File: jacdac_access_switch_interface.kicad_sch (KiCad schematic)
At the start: 43 parts

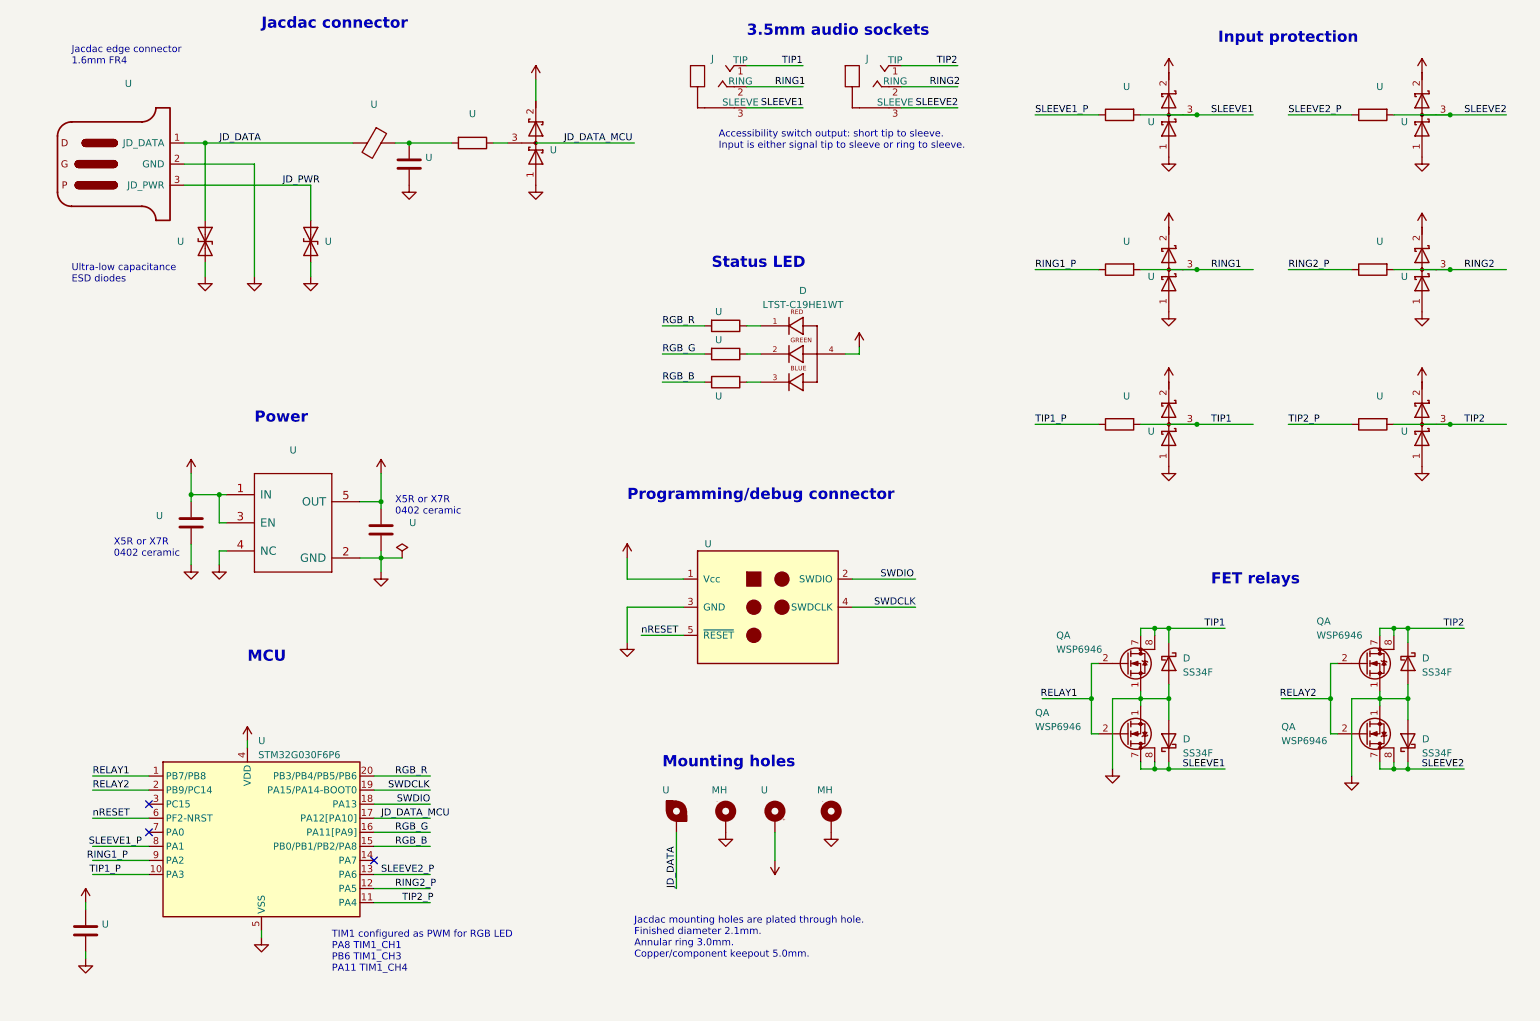
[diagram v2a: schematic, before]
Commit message: Added push button switch to enable flashing & orange status LED
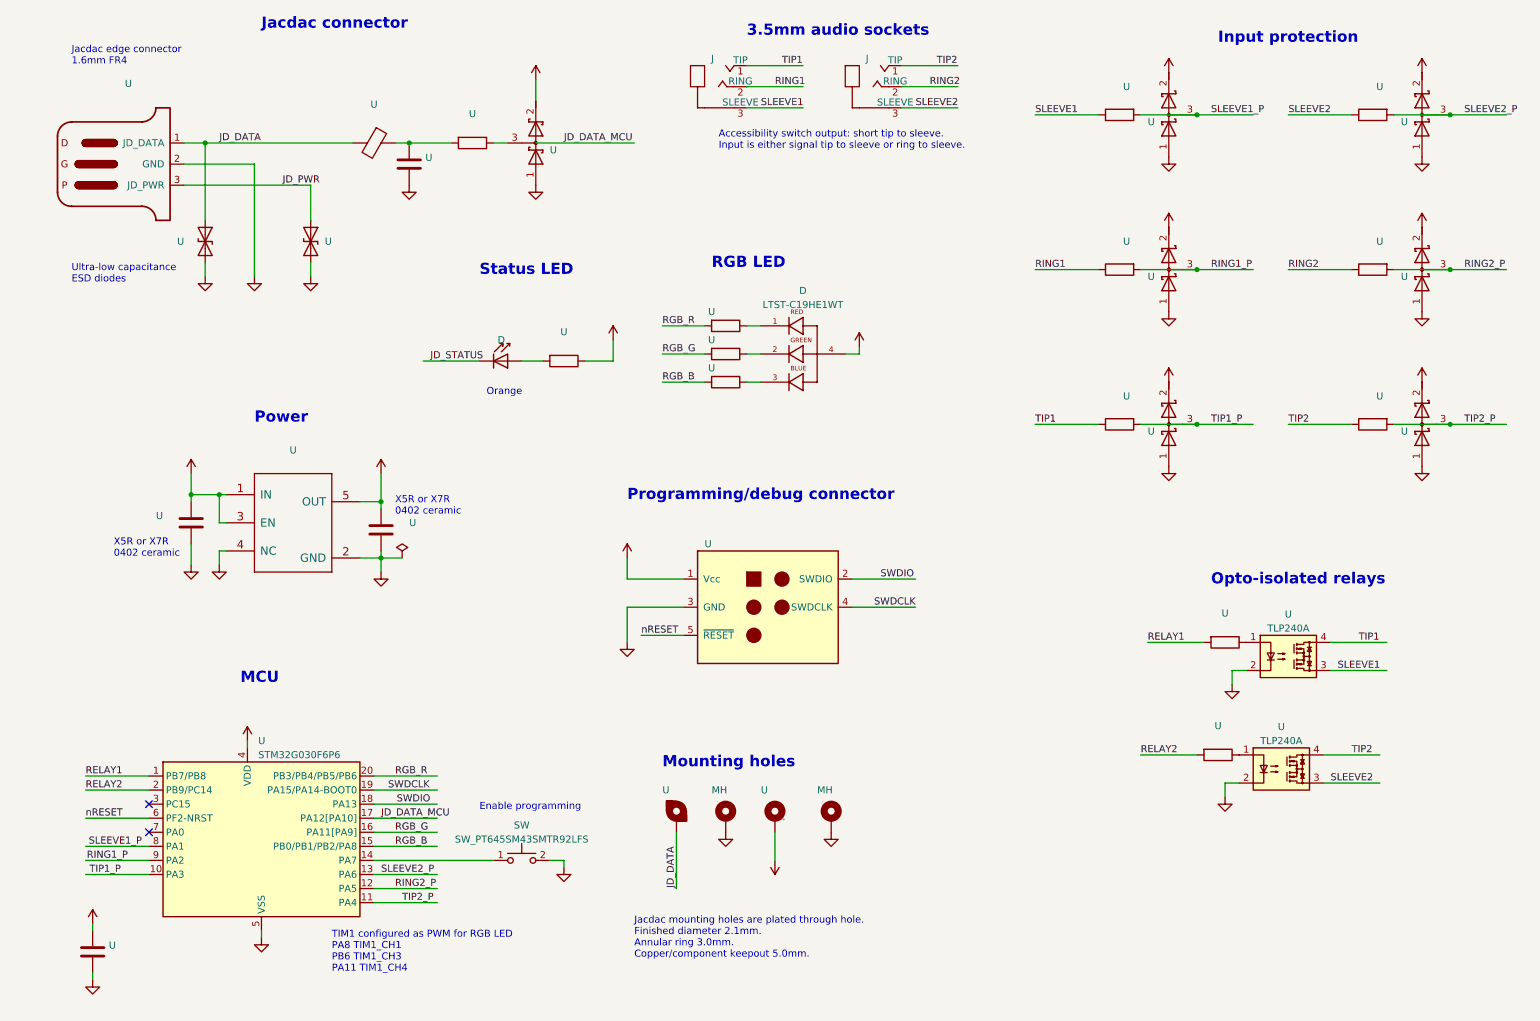
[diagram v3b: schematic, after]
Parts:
- removed D (x4): SS34F, jacdac_access_switch_interface:SMAF, symbol jacdac_access_switch_interface:SS34F
- removed Q (x4): WSP6946, jacdac_access_switch_interface:SOP-8_3.9x4.9mm_P1.27mm, symbol jacdac_access_switch_interface:WSP6946
- added D: LED_status, jacdac_access_switch_interface:LED_0603_1608Metric, symbol jacdac_access_switch_interface:LED_status
- added SW: SW_PT645SM43SMTR92LFS, jacdac_access_switch_interface:SW_SPST_PTS645, symbol jacdac_access_switch_interface:SW_PT645SM43SMTR92LFS
- added U (x3): (no value), symbol Device:R
- added U (x2): TLP240A, jacdac_access_switch_interface:LF1_TP1_TOSHIBA_11-5B201S, symbol jacdac_access_switch_interface:TLP240A
- U: LCSC C270649 -> C25105
- U: LCSC C270649 -> C25756
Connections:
- net +3V3: now also U.1
- net GND: now also SW.2, U.2, U.2
- net RELAY1: now also U.2
- net RELAY2: now also U.2
- net RING1: now also U.1; no longer U.2, U.3 (common)
- net RING1_P: now also U.2, U.3 (common); no longer U.1
- net RING2: now also U.1; no longer U.2, U.3 (common)
- net RING2_P: now also U.2, U.3 (common); no longer U.1
- net SLEEVE1: now also U.1, U.3; no longer U.2, U.3 (common)
- net SLEEVE1_P: now also U.2, U.3 (common); no longer U.1
- net SLEEVE2: now also U.1, U.3; no longer U.2, U.3 (common)
- net SLEEVE2_P: now also U.2, U.3 (common); no longer U.1
- net TIP1: now also U.1, U.4; no longer U.2, U.3 (common)
- net TIP1_P: now also U.2, U.3 (common); no longer U.1
- net TIP2: now also U.1, U.4; no longer U.2, U.3 (common)
- net TIP2_P: now also U.2, U.3 (common); no longer U.1
- net at U.14 (PA7): now also SW.1
- new net: D.2 (A), U.2
- new net: U.1, U.1 (x2)
- new net JD_STATUS: D.1 (K)
- no-connect marks 3 -> 2
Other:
- note added: "Enable programming"
- note added: "Opto-isolated relays"
- note added: "Orange"
- note added: "RGB LED"
- note removed: "FET relays"
- moved on the sheet: U

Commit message: Initial component placement for PCB
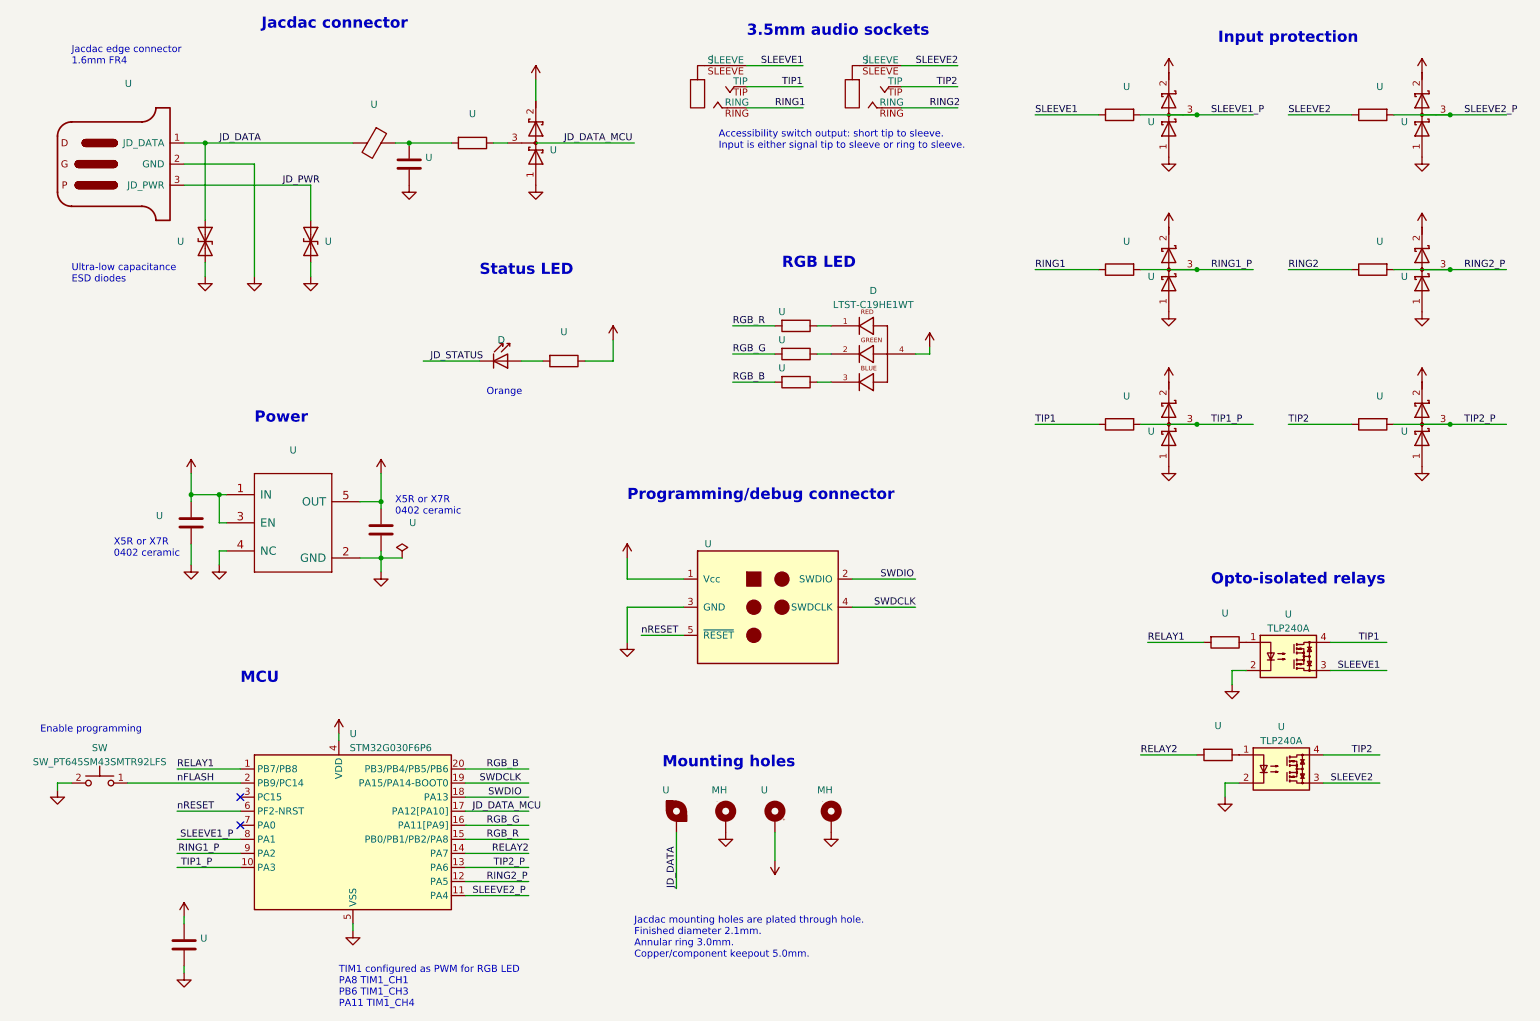
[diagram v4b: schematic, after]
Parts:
- removed J (x2): 54-00036_audio_plug, jacdac_access_switch_interface:Tensility-54-00036-0, symbol jacdac_access_switch_interface:54-00036_audio_plug
- added J (x2): jack_3.5_pj313d, jacdac_access_switch_interface:jack_3.5_pj313d_smt, symbol jacdac_access_switch_interface:jack_3.5_pj313d
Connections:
- net RELAY2: now also U.14 (PA7); no longer U.2 (PB9/PC14)
- net RGB_B: now also U.20 (PB3/PB4/PB5/PB6); no longer U.15 (PB0/PB1/PB2/PA8)
- net RGB_R: now also U.15 (PB0/PB1/PB2/PA8); no longer U.20 (PB3/PB4/PB5/PB6)
- net RING1: now also J.RING
- net RING2: now also J.RING
- net SLEEVE1: now also J.SLEEVE
- net SLEEVE2: now also J.SLEEVE
- net SLEEVE2_P: now also U.11 (PA4); no longer U.13 (PA6)
- net TIP1: now also J.TIP
- net TIP2: now also J.TIP
- net TIP2_P: now also U.13 (PA6); no longer U.11 (PA4)
- net nFLASH: now reaches SW.1
- net nFLASH: now also U.2 (PB9/PC14); no longer U.14 (PA7)
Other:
- moved on the sheet: D, SW, U

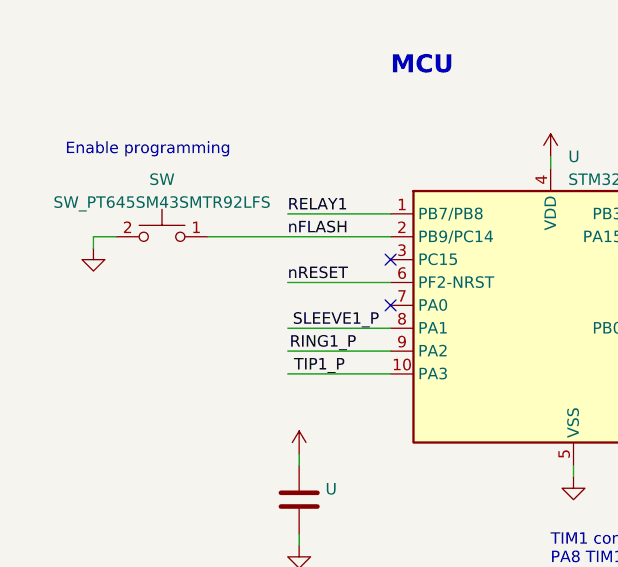
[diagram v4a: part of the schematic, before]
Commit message: Updated footprint identifiers, routing started
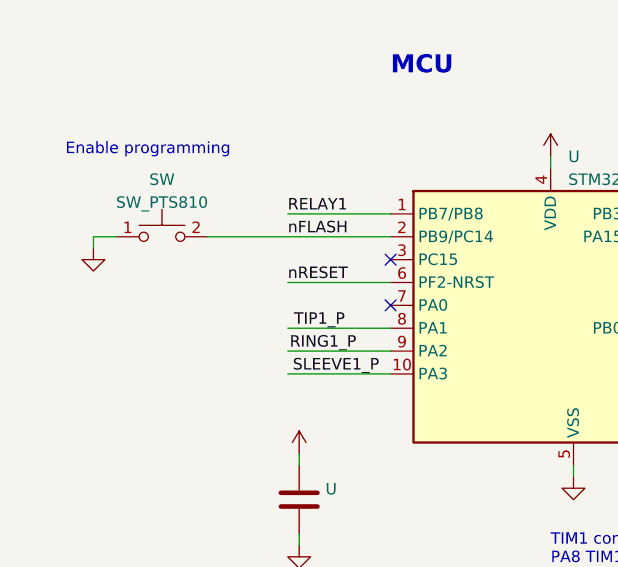
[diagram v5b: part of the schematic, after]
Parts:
- removed SW: SW_PT645SM43SMTR92LFS, jacdac_access_switch_interface:SW_SPST_PTS645, symbol jacdac_access_switch_interface:SW_PT645SM43SMTR92LFS
- added SW: SW_PTS810, jacdac_access_switch_interface:SW_SPST_PTS810, symbol jacdac_access_switch_interface:SW_PTS810
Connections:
- net GND: now also SW.1
- net SLEEVE1_P: now also U.10 (PA3); no longer U.8 (PA1)
- net TIP1_P: now also U.8 (PA1); no longer U.10 (PA3)
- net nFLASH: now also SW.2

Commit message: Routing in progress
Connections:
- net RELAY2: now also U.11 (PA4); no longer U.14 (PA7)
- net RING2_P: now also U.13 (PA6); no longer U.12 (PA5)
- net SLEEVE1: now also U.4; no longer U.3
- net SLEEVE2_P: now also U.12 (PA5); no longer U.11 (PA4)
- net TIP1: now also U.3; no longer U.4
- net TIP2_P: now also U.14 (PA7); no longer U.13 (PA6)

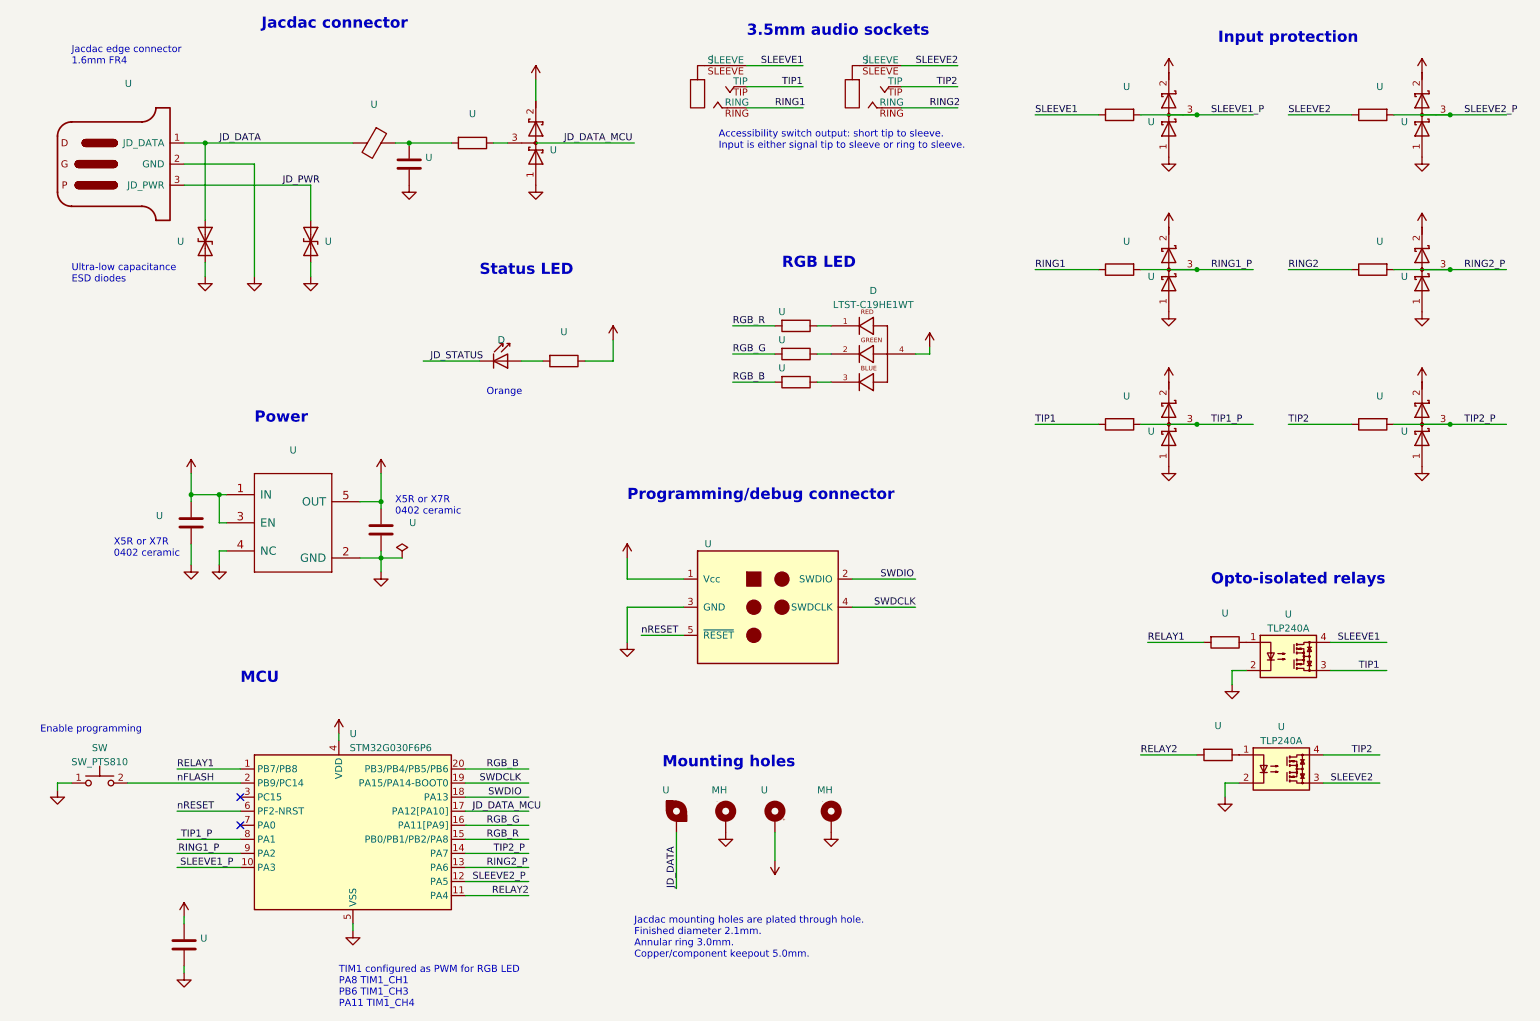
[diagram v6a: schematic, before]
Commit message: Last commit before re-assigning pins on MCU and spinning MCU
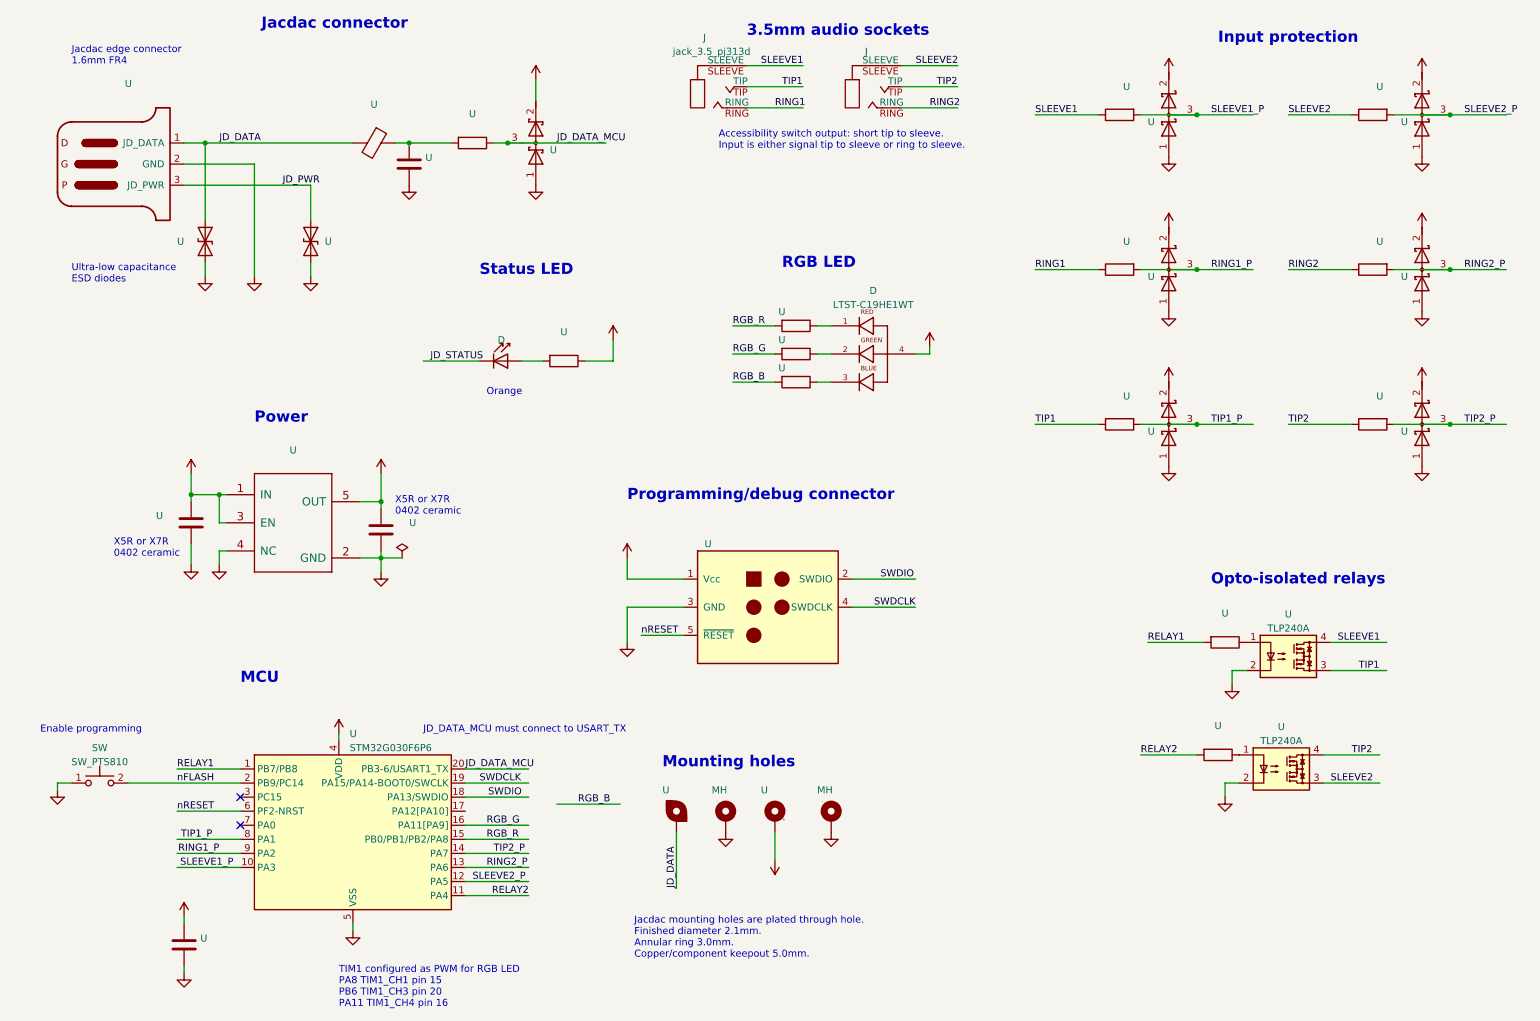
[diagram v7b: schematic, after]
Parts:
- J: symbol jacdac_access_switch_interface:jack_3.5_pj313d -> jacdac_access_switch_interface:jack_3.5mm_PJ313D
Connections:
- net JD_DATA_MCU: now also U.1, U.20 (PB3-6/USART1_TX), U.3 (common); no longer U.17 (PA12[PA10])
- net RGB_B: no longer U.20 (PB3/PB4/PB5/PB6)
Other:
- note added: "JD_DATA_MCU must connect to USART_TX"
- note added: "TIM1 configured as PWM for RGB LED PA8 TIM1_CH1 pin 15 PB6 TIM1_CH3 pin 20 PA11 TIM1_CH4 pin 16"
- note removed: "TIM1 configured as PWM for RGB LED PA8 TIM1_CH1 PB6 TIM1_CH3 PA11 TIM1_CH4"
